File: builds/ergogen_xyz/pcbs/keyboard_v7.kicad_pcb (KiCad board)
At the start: 2 copper layers, 248 x 123.7 mm, 76 parts

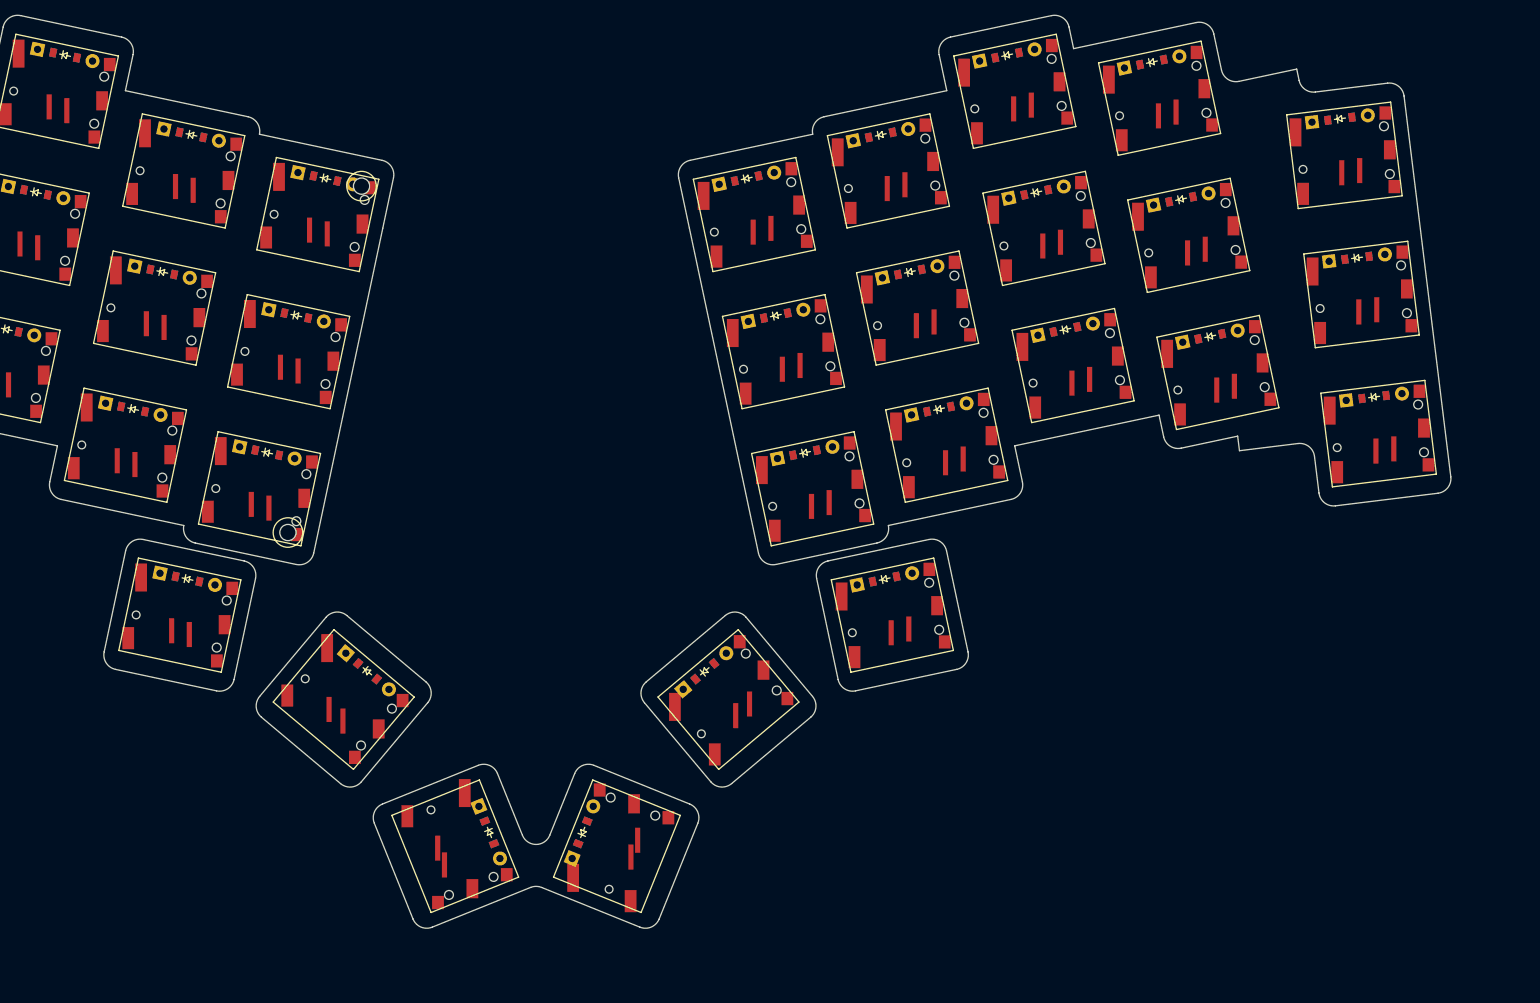
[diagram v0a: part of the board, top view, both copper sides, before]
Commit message: Redesign: cables + hinge folding, thumb support, MCU in 3D, thinner
Design changes per updated requirements:
- Remove tenting mechanism, replace with two horizontal cables
  (top Q-P, bottom Z-M) connecting halves with hook quick-detach
- Add lockable ball bearing hinge at center for folding
- Fix thumb cluster: bridge outlines so frame/plate/PCB cover all
  thumb keys (no more floating keys)
- Add nice!nano MCU + USB-C to 3D assembly model
- Reduce thickness from 7.3mm to 3.8mm by removing standoffs,
  thinning plates (1.0mm bottom, 1.2mm switch plate)
- assembly.scad is now the interactive viewer (openscad with
  rotate/zoom/cross-section), not just static PNG
- Update BOM: replace turnbuckle tenting with cables/hooks/hinge
- Update render.md with interactive viewer instructions

Co-Authored-By: Claude Opus 4.6 <noreply@anthropic.com>
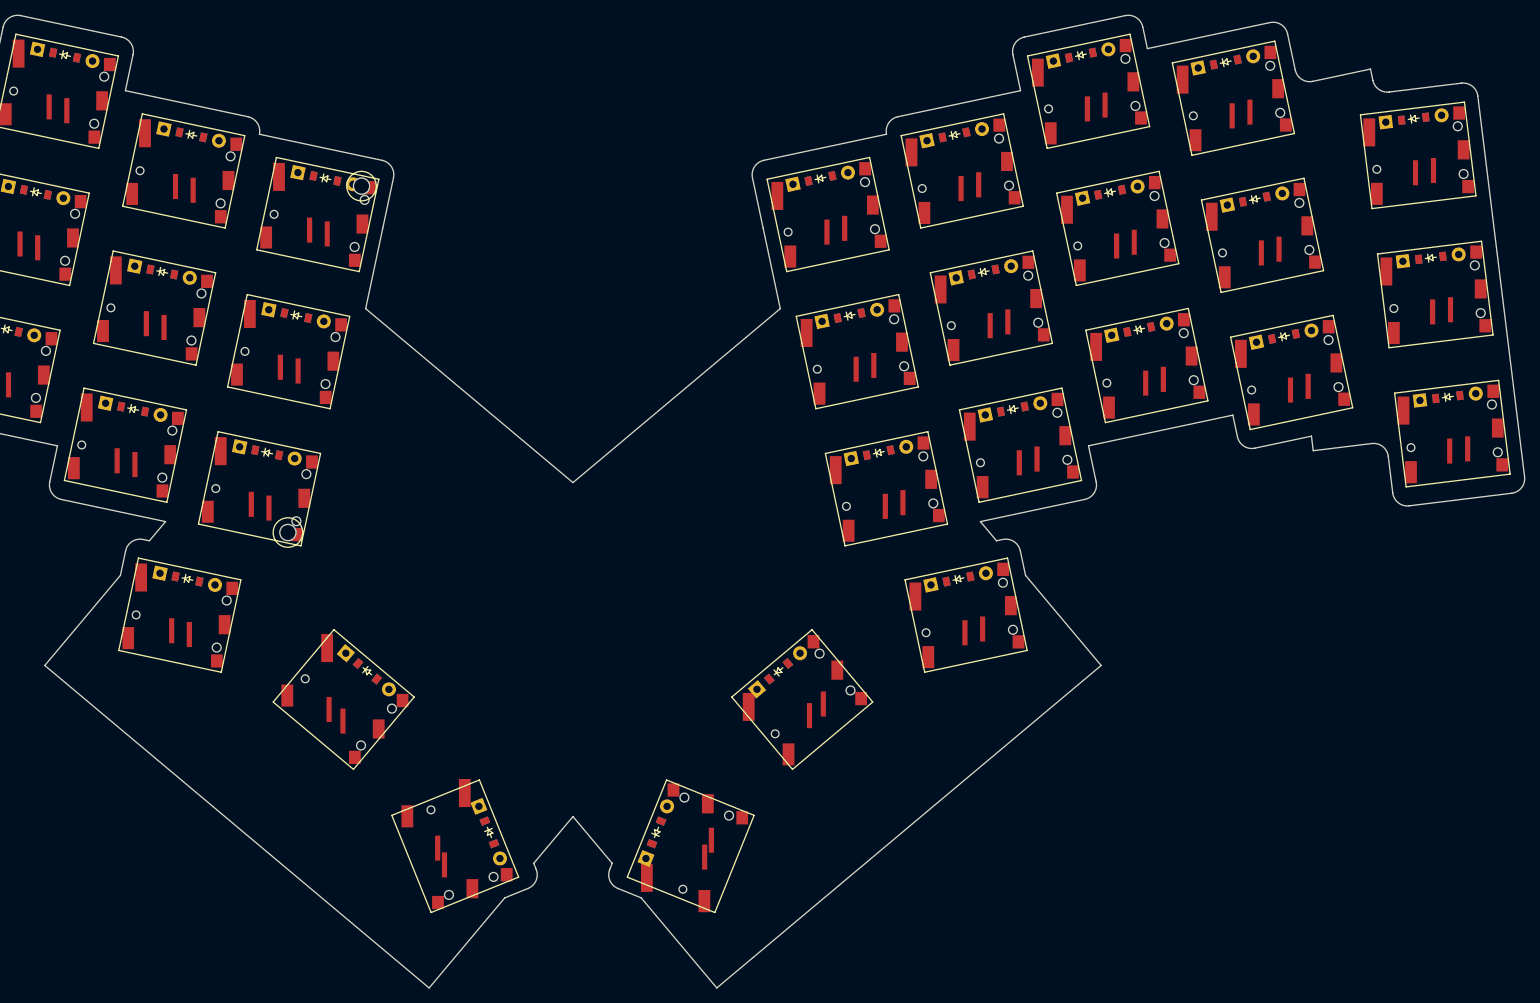
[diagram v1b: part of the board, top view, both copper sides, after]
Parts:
- moved D19 10.0 mm to (237.8, -4.96)
- moved D20 10.0 mm to (235.5, -23.8)
- moved D21 10.0 mm to (233.1, -42.7)
- moved D22 10.0 mm to (215.6, -13.2)
- moved D23 10.0 mm to (211.6, -31.8)
- moved D24 10.0 mm to (207.7, -50.3)
- moved D25 10.0 mm to (195.9, -14.1)
- moved D26 10.0 mm to (192.0, -32.7)
- moved D27 10.0 mm to (188.0, -51.3)
- moved D28 10.0 mm to (178.8, -3.32)
- moved D29 10.0 mm to (174.9, -21.9)
- moved D30 10.0 mm to (170.9, -40.5)
- moved D31 10.0 mm to (160.6, 2.58)
- moved D32 10.0 mm to (156.7, -16.0)
- moved D33 10.0 mm to (152.7, -34.6)
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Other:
- board size 248 x 123.7 mm -> 258 x 131.8 mm
